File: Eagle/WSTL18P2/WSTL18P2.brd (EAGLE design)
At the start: 22.9 x 22.9 mm, 21 parts, among them CON1 1X6CONN-1.27-ROUND, CON2 1X6CONN-1.27-ROUND, CON3 1X6CONN-1.27-ROUND, CON4 1X6CONN-1.27-ROUND, T1 ABS07AIG

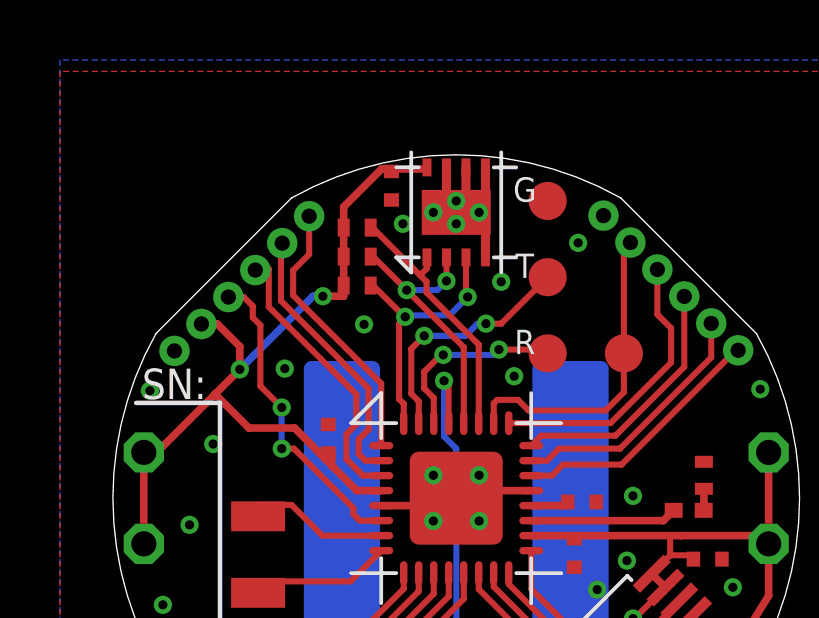
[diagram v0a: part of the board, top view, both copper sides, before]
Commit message: Adding 1.27mm headers to TWI (I2C) lines.
This will make the TWI accessible to expansion shields.
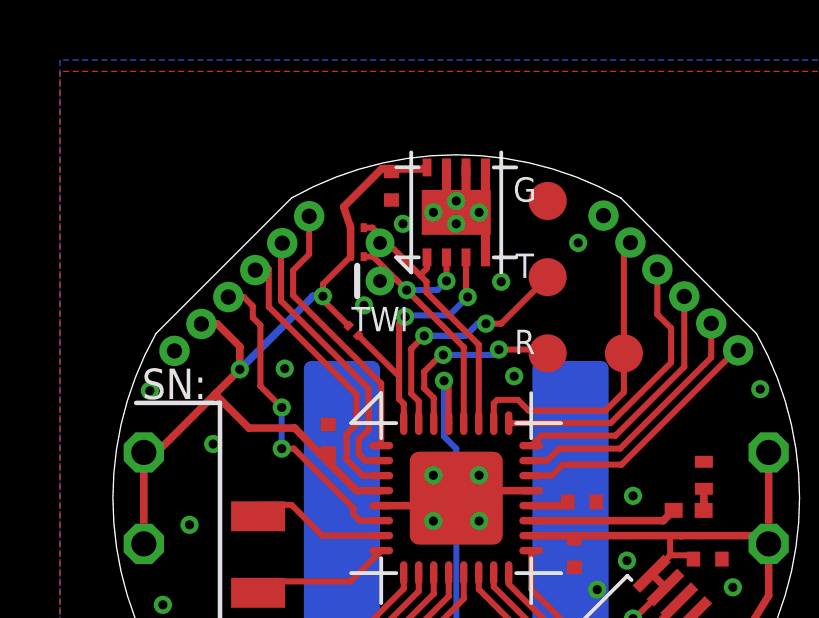
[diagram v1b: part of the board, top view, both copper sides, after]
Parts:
- added TWI: 1X2CONN1.27, AVR_ISP_127:1X2_1.27
- R2, R3, R4: device Passives:RES_0402 -> Passives:RES_CAP_0201
- moved R4 1.50 mm to (9.78, 18.8), turned to 315 degrees
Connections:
- net SCL0: now also TWI.1
- net SDA0: now also TWI.2
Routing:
- net VCC: track 53.9 -> 55.0 mm
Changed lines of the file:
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@@
 <attribute name="NAME" x="21.59" y="12.065" size="0.8128" layer="51" font="vector" ratio="10" align="center"/>
 </element>
-<element name="R2" library="Passives" package="RES_0402" value="4.7k" x="9.906" y="22.225" smashed="yes">
+<element name="R2" library="Passives" package="RES_CAP_0201" value="4.7k" x="9.906" y="22.225" smashed="yes">
 <attribute name="NAME" x="8.509" y="22.225" size="0.8128" layer="51" font="vector" ratio="10" align="center"/>
 </element>
-<element name="R3" library="Passives" package="RES_0402" value="4.7k" x="9.906" y="21.2598" smashed="yes">
+<element name="R3" library="Passives" package="RES_CAP_0201" value="4.7k" x="9.906" y="21.2598" smashed="yes">
 <attribute name="NAME" x="8.509" y="21.2598" size="0.8128" layer="51" font="vector" ratio="10" align="center"/>
 </element>
@@
 <attribute name="NAME" x="22.352" y="13.97" size="0.8128" layer="51" font="vector" ratio="10" rot="R270" align="center"/>
 </element>
-<element name="R4" library="Passives" package="RES_0402" value="4.7k" x="9.906" y="20.2946" smashed="yes">
-<attribute name="NAME" x="8.255" y="20.294596875" size="0.8128" layer="51" font="vector" ratio="12" align="center"/>
+<element name="R4" library="Passives" package="RES_CAP_0201" value="4.7k" x="9.779" y="18.796" smashed="yes" rot="R315">
+<attribute name="NAME" x="8.6115625" y="19.963428125" size="0.8128" layer="51" font="vector" ratio="12" rot="R315" align="center"/>
 </element>
 <element name="CON1" library="AVR_ISP_127" package="1X6_1.27_ROUND" value="1X6CONN-1.27-ROUND" x="22.606" y="8.3058" smashed="yes" rot="R225">
@@
 <element name="UART" library="Connectors" package="4_PIN_0.1INCH_POGO_PADS_ANGLE" value="4_PIN_0.1_INCH_POGO_CONN_ANGLE" x="16.256" y="18.034" smashed="yes" rot="R270"/>
 <element name="U$1" library="Battery_holders" package="CR2032-LINX-M-THM" value="LINX-CR2032-BAT-HLD-M-THM" x="13.208" y="13.208" rot="MR0"/>
+<element name="TWI" library="AVR_ISP_127" package="1X2_1.27" value="1X2CONN1.27" x="10.668" y="20.447" rot="R90"/>
 </elements>
 <signals>
@@
 <wire x1="12.233" y1="20.869" x2="12.0015" y2="20.6375" width="0.2032" layer="1"/>
 <wire x1="12.0015" y1="20.6375" x2="10.414" y2="22.225" width="0.2032" layer="1"/>
-<wire x1="10.414" y1="22.225" x2="10.356" y2="22.225" width="0.2032" layer="1"/>
+<wire x1="10.414" y1="22.225" x2="10.126" y2="22.225" width="0.2032" layer="1"/>
 <wire x1="13.958" y1="18.3254" x2="12.2174" y2="20.066" width="0.2032" layer="1"/>
 <wire x1="12.2174" y1="20.066" x2="12.2174" y2="20.4216" width="0.2032" layer="1"/>
 <wire x1="12.2174" y1="20.4216" x2="12.0015" y2="20.6375" width="0.2032" layer="1"/>
+<contactref element="TWI" pad="2"/>
+<wire x1="10.414" y1="22.225" x2="10.668" y2="21.717" width="0" layer="19" extent="1-1"/>
 </signal>
 <signal name="SCL0" class="2">
@@
 <wire x1="13.458" y1="18.2412" x2="11.557" y2="20.1422" width="0.2032" layer="1"/>
 <wire x1="11.557" y1="20.1422" x2="10.4394" y2="21.2598" width="0.2032" layer="1"/>
-<wire x1="10.4394" y1="21.2598" x2="10.356" y2="21.2598" width="0.2032" layer="1"/>
+<wire x1="10.4394" y1="21.2598" x2="10.126" y2="21.2598" width="0.2032" layer="1"/>
 <wire x1="11.557" y1="20.1422" x2="12.5782" y2="20.1422" width="0.2032" layer="16"/>
 <wire x1="12.5782" y1="20.1422" x2="12.883" y2="20.447" width="0.2032" layer="16"/>
+<contactref element="TWI" pad="1"/>
+<wire x1="10.4394" y1="21.2598" x2="10.668" y2="20.447" width="0" layer="19" extent="1-1"/>
 </signal>
 <signal name="RESET" class="2">
@@
 <contactref element="R1" pad="1"/>
 <via x="8.763" y="19.939" extent="1-16" drill="0.3048" shape="octagon"/>
-<wire x1="9.456" y1="21.2598" x2="9.456" y2="22.225" width="0.254" layer="1"/>
-<wire x1="9.456" y1="22.225" x2="9.456" y2="22.918" width="0.254" layer="1"/>
+<wire x1="9.686" y1="21.2598" x2="9.686" y2="22.225" width="0.254" layer="1"/>
+<wire x1="9.686" y1="22.225" x2="9.456" y2="22.918" width="0.254" layer="1"/>
 <wire x1="9.456" y1="22.918" x2="10.7202" y2="24.1822" width="0.254" layer="1"/>
 <wire x1="12.233" y1="24.233" x2="12.1822" y2="24.1822" width="0.254" layer="1"/>
@@
 <wire x1="5.9944" y1="17.5006" x2="5.1689" y2="16.6751" width="0.254" layer="1"/>
 <wire x1="6.2992" y1="15.5448" x2="5.1689" y2="16.6751" width="0.254" layer="1"/>
-<wire x1="9.456" y1="19.939" x2="9.456" y2="20.2946" width="0.254" layer="1"/>
-<wire x1="9.456" y1="20.2946" x2="9.456" y2="21.2598" width="0.254" layer="1"/>
 <wire x1="5.9944" y1="17.5006" x2="8.4328" y2="19.939" width="0.254" layer="16"/>
 <wire x1="8.4328" y1="19.939" x2="8.763" y2="19.939" width="0.254" layer="16"/>
-<wire x1="8.763" y1="19.939" x2="9.456" y2="19.939" width="0.254" layer="1"/>
 <wire x1="23.622" y1="9.9568" x2="22.606" y2="8.3058" width="0.254" layer="1"/>
 <wire x1="4.713696875" y1="19.013896875" x2="5.243103125" y2="19.013896875" width="0.254" layer="1"/>
@@
 <wire x1="18.034" y1="7.112" x2="19.1008" y2="8.1788" width="0.2032" layer="16"/>
 <wire x1="19.1008" y1="8.1788" x2="19.1008" y2="9.1948" width="0.2032" layer="16"/>
+<wire x1="8.763" y1="19.939" x2="8.763" y2="20.3368" width="0.2032" layer="1"/>
+<wire x1="8.763" y1="20.3368" x2="9.686" y2="21.2598" width="0.2032" layer="1"/>
+<wire x1="8.763" y1="19.939" x2="8.763" y2="19.811996875" width="0.2032" layer="1"/>
+<wire x1="8.763" y1="19.811996875" x2="9.623434375" y2="18.9515625" width="0.2032" layer="1"/>
 <wire x1="10.708" y1="13.458" x2="15.708" y2="11.958" width="0" layer="19" extent="1-1"/>
 </signal>
@@
 <wire x1="12.696" y1="13.208" x2="13.208" y2="13.208" width="0.254" layer="1"/>
 <contactref element="R5" pad="2"/>
-<via x="10.1346" y="18.9992" extent="1-16" drill="0.3048"/>
+<via x="10.1346" y="19.6342" extent="1-16" drill="0.3048"/>
 <contactref element="CON1" pad="2"/>
 <via x="22.4282" y="10.2362" extent="1-16" drill="0.3048"/>
@@
 <contactref element="UART" pad="4"/>
 <wire x1="13.97" y1="22.733" x2="13.97" y2="23.114" width="0" layer="19" extent="1-1"/>
+<wire x1="11.049" y1="23.147" x2="11.43" y2="22.352" width="0" layer="19" extent="1-1"/>
 </signal>
 <signal name="N$3">
@@
 <wire x1="11.5062" y1="19.2532" x2="11.557" y2="19.304" width="0.2032" layer="16"/>
 <wire x1="11.5062" y1="19.2532" x2="11.4808" y2="19.2532" width="0.2032" layer="1"/>
-<wire x1="11.4808" y1="19.2532" x2="10.4394" y2="20.2946" width="0.2032" layer="1"/>
-<wire x1="10.4394" y1="20.2946" x2="10.356" y2="20.2946" width="0.2032" layer="1"/>
-<wire x1="11.303" y1="16.51" x2="11.303" y2="19.0246" width="0.2032" layer="1"/>
+<wire x1="11.303" y1="16.51" x2="11.303" y2="17.145" width="0.2032" layer="1"/>
+<wire x1="11.303" y1="17.271996875" x2="11.303" y2="19.0246" width="0.2032" layer="1"/>
 <wire x1="11.303" y1="19.0246" x2="11.5062" y2="19.2532" width="0.2032" layer="1"/>
 <wire x1="13.533" y1="21.233" x2="13.533" y2="19.9846" width="0.2032" layer="1"/>
@@
 <wire x1="11.557" y1="19.304" x2="12.9794" y2="19.304" width="0.2032" layer="16"/>
 <wire x1="12.9794" y1="19.304" x2="13.589" y2="19.9136" width="0.2032" layer="16"/>
+<wire x1="9.9345625" y1="18.640434375" x2="11.303" y2="17.271996875" width="0.2032" layer="1"/>
+<wire x1="11.303" y1="17.271996875" x2="11.303" y2="17.145" width="0.2032" layer="1"/>
 </signal>
 <signal name="N$4">

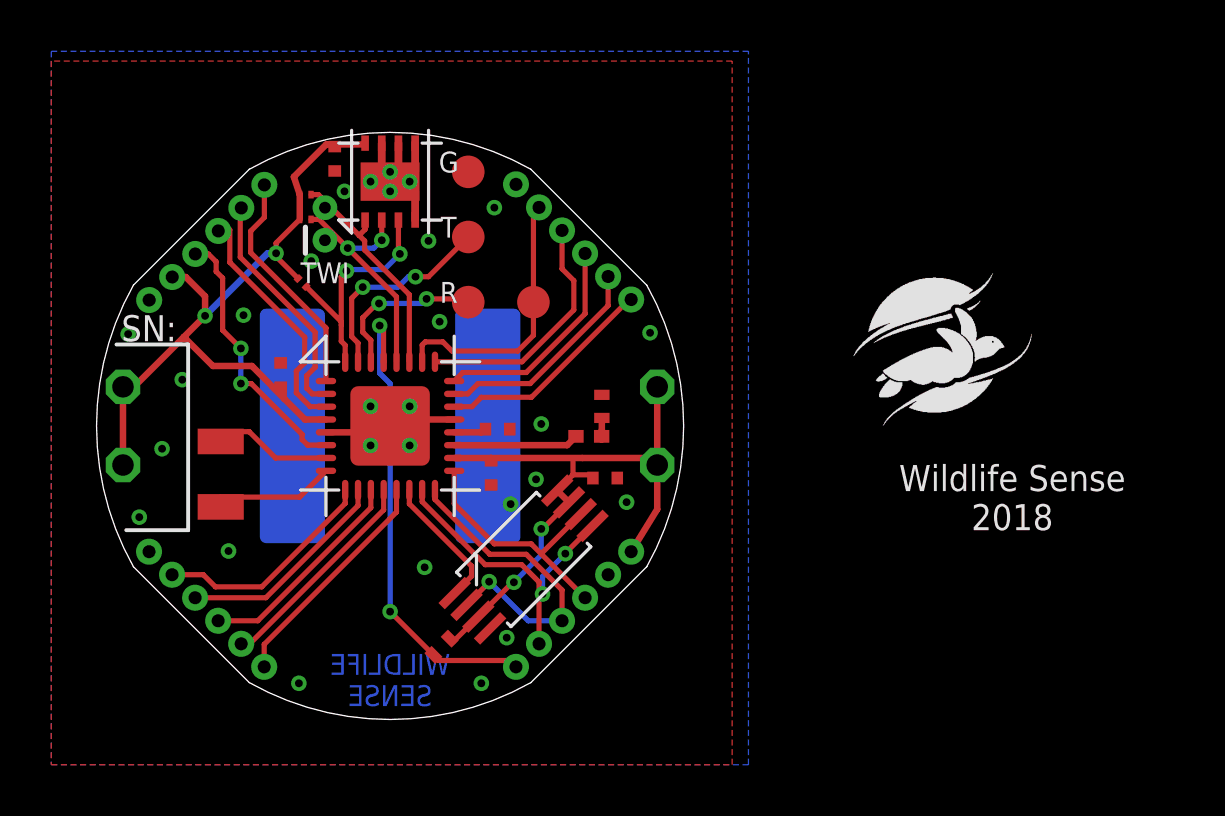
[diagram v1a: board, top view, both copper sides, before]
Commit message: Reducing signal trace widths towards 6mil
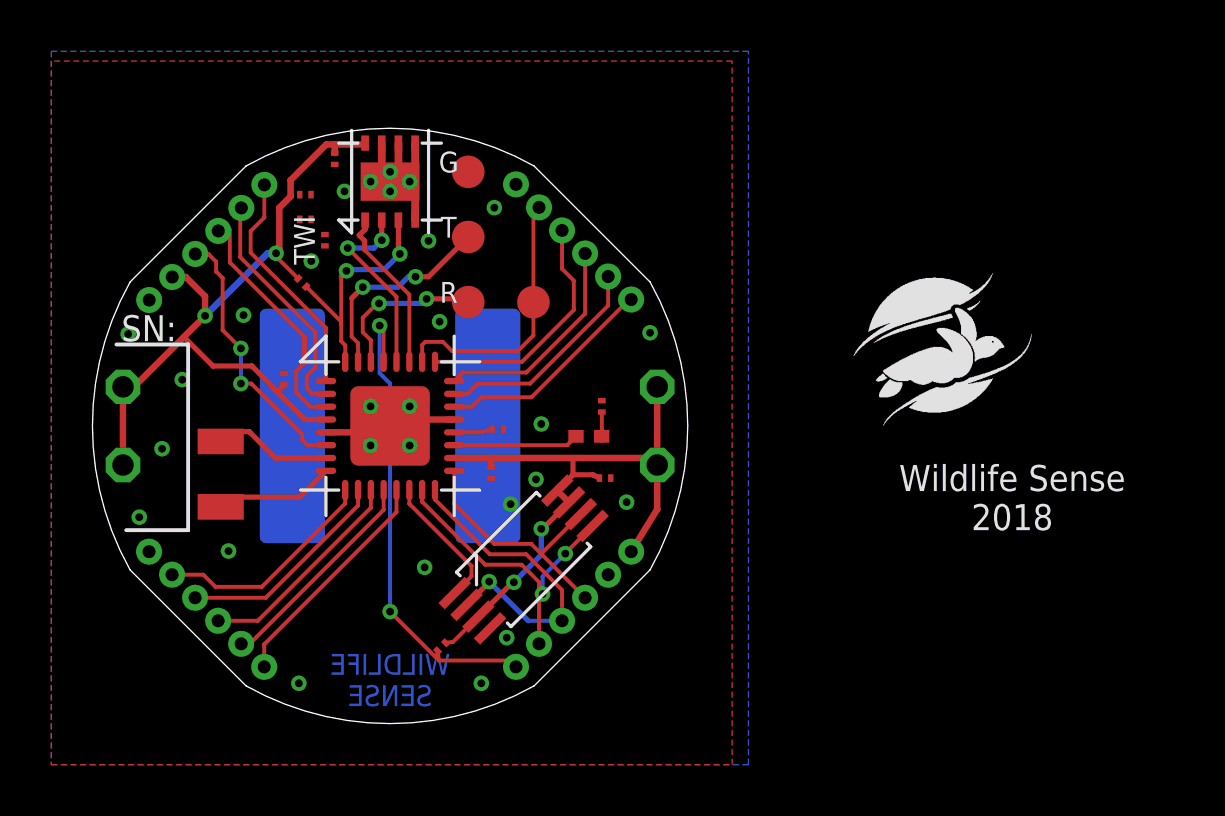
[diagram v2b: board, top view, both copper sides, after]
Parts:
- C1, C2, C3, C4, C5: device Passives:CAP_0402 -> Passives:RES_CAP_0201
- R1, R5: device Passives:RES_0402 -> Passives:RES_CAP_0201
- TWI: value 1X2CONN1.27 -> CAP_0201_CERAMIC; device AVR_ISP_127:1X2_1.27 -> Passives:RES_CAP_0201
- moved C1 0.20 mm to (9.07, 15.0)
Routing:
- net SDA0: track 8.96 -> 6.43 mm
- net SCL0: track 9.35 -> 7.46 mm
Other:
- board size 22.9 x 22.9 mm -> 23.2 x 23.2 mm

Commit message: Changing signal traces to 6 mil
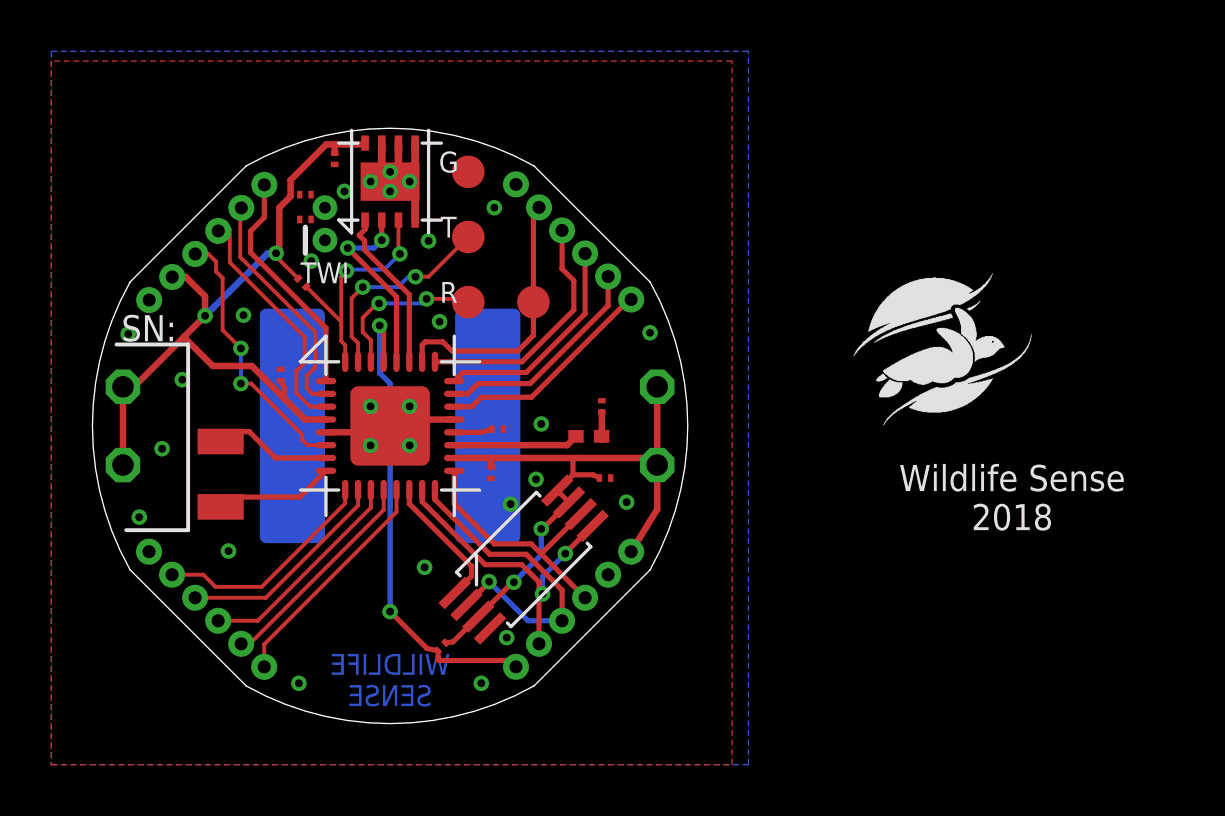
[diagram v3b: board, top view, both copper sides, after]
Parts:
- TWI: value CAP_0201_CERAMIC -> 1X2CONN1.27; device Passives:RES_CAP_0201 -> AVR_ISP_127:1X2_1.27
- moved C1 0.20 mm to (8.94, 15.2)

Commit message: More routing optimizations and changing trances to 6 mil.
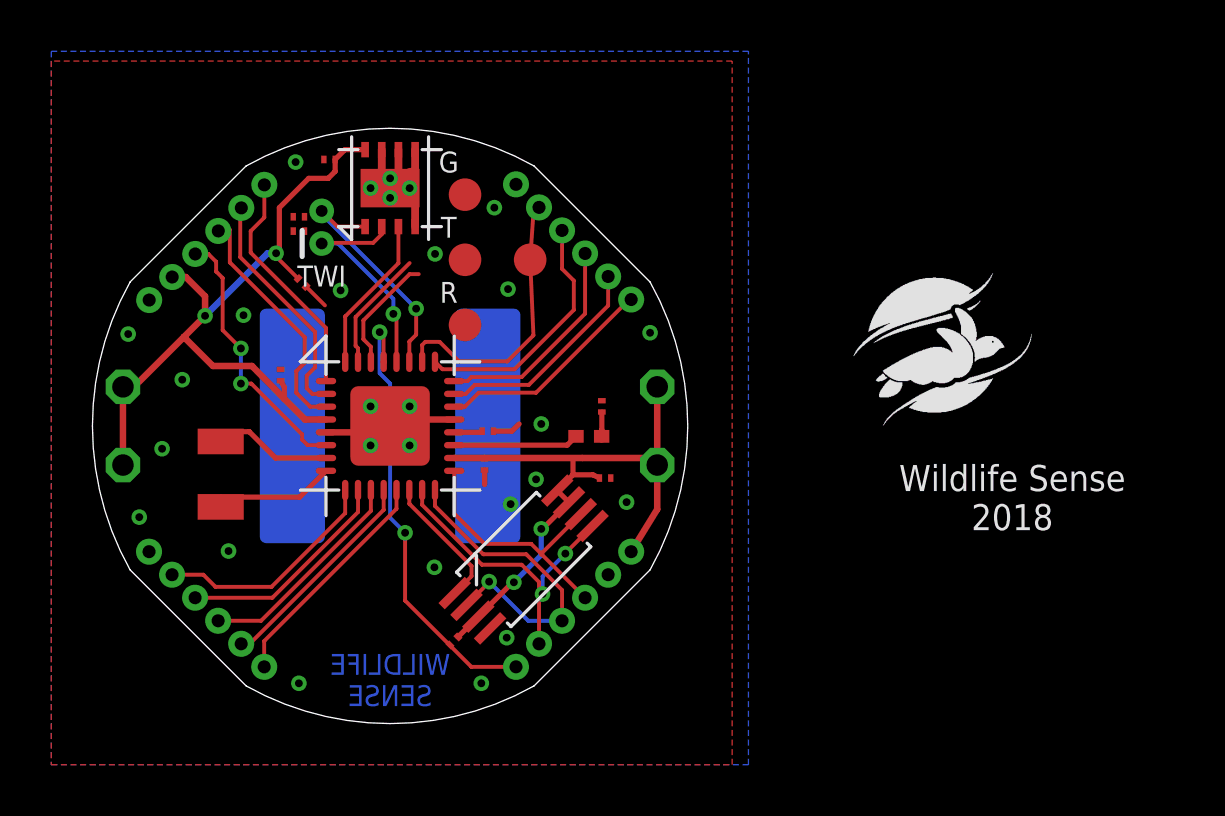
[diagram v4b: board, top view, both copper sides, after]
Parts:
- moved R2 0.90 mm to (9.65, 21.4)
- moved UART 0.90 mm to (16.1, 17.1)
- moved R1 0.53 mm to (15.7, 4.83)
- moved R3 0.52 mm to (9.65, 20.8)
- moved C2 0.42 mm to (16.9, 11.7)
- moved C3 0.39 mm to (17.0, 13.0)
- moved TMP 0.25 mm to (13.2, 22.5)
- moved C4 0.20 mm to (10.8, 23.6), turned to 180 degrees
- moved TWI 0.18 mm to (10.5, 20.3)
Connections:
- net N$3 renamed AREF
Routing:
- net TXD0: track 8.12 -> 4.76 mm, vias 2 -> 0
- net SDA0: track 6.43 -> 9.46 mm, vias 0 -> 1
- net TMP_INT: track 9.34 -> 7.17 mm, vias 2 -> 0
- net RXD0: track 6.32 -> 4.64 mm, vias 2 -> 0
- net SCL0: track 7.46 -> 8.98 mm, vias 2 -> 1
- net VCC: track 55.8 -> 54.3 mm
- net GND: track 11.4 -> 12.8 mm
- net RESET: track 18.7 -> 17.5 mm
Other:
- board text removed: "SN:"

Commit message: Making TWI (I2C) pins available on perimeter headers
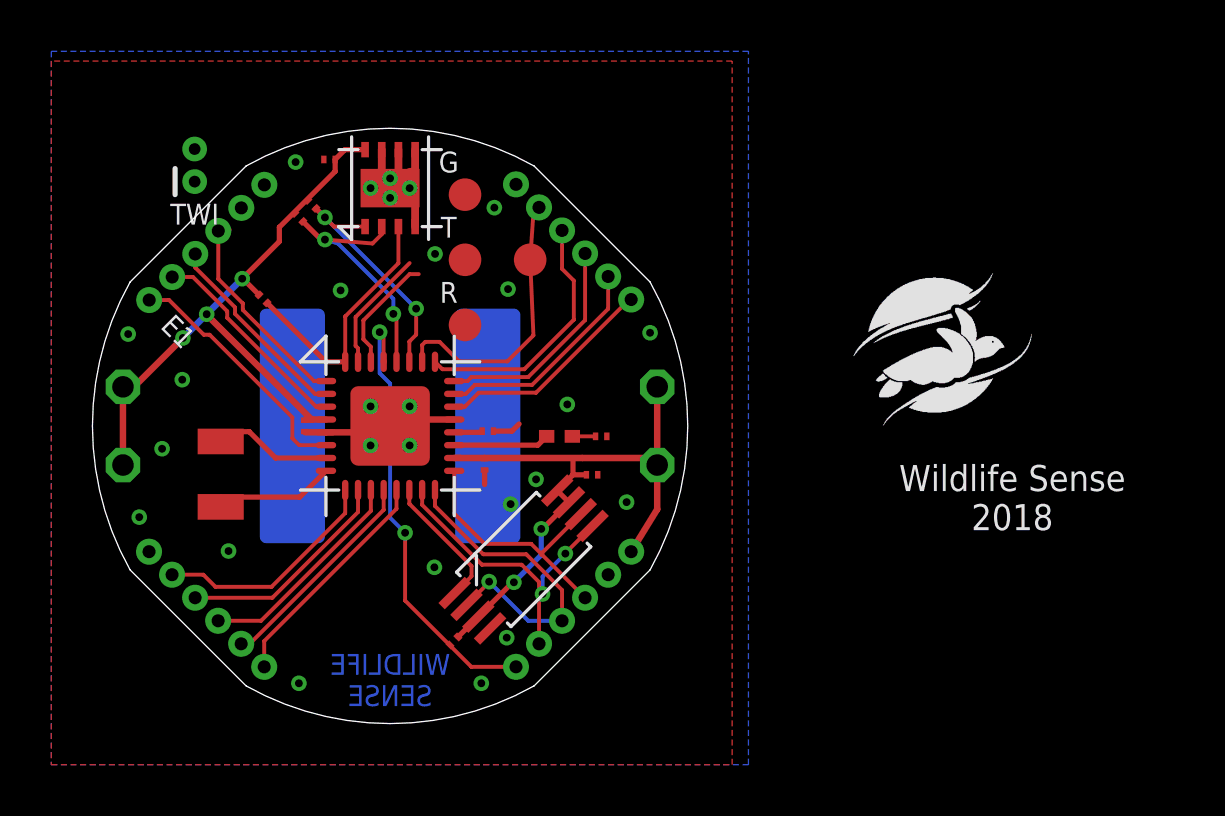
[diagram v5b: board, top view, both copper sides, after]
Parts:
- moved TWI 5.51 mm to (5.59, 22.7)
- moved C1 2.19 mm to (9.88, 13.2), turned to 270 degrees
- moved R4 1.65 mm to (8.26, 18.2)
- moved R5 1.17 mm to (21.4, 12.8), turned to 0 degrees
- moved LED0 1.14 mm to (19.8, 12.8)
- moved R2 0.70 mm to (10.2, 21.8), turned to 315 degrees
- moved R3 0.53 mm to (9.65, 21.3), turned to 315 degrees
- moved C5 0.52 mm to (21.1, 11.3)
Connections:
- net GND: no longer CON4.6
- net PD3: now also CON4.3; no longer CON4.1
- net PD4: now also CON4.4; no longer CON4.2
- net PE0: now also CON4.5; no longer CON4.3
- net PE1: now also CON4.6; no longer CON4.4
- net SCL0: no longer TWI.1
- net SDA0: no longer TWI.2
- net VCC: no longer CON4.5
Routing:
- net VCC: track 54.3 -> 49.4 mm, vias 4 -> 5
- net TMP_INT: track 7.17 -> 10.1 mm
- net PD4: track 9.32 -> 7.81 mm
- net PE2: track 5.00 -> 3.75 mm
- net PD3: track 9.08 -> 7.87 mm
- net PE0: track 9.73 -> 8.54 mm
- net SCL0: track 8.98 -> 9.91 mm, vias 1 -> 2
- net GND: track 12.8 -> 13.7 mm, vias 28 -> 27
- net PE1: track 10.5 -> 9.71 mm, vias 2 -> 0
- net SDA0: track 9.46 -> 9.42 mm, vias 1 -> 2
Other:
- board text added: "E1"
